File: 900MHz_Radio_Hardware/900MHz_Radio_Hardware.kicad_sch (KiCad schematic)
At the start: 9 parts, among them U1 TSR_1-2450

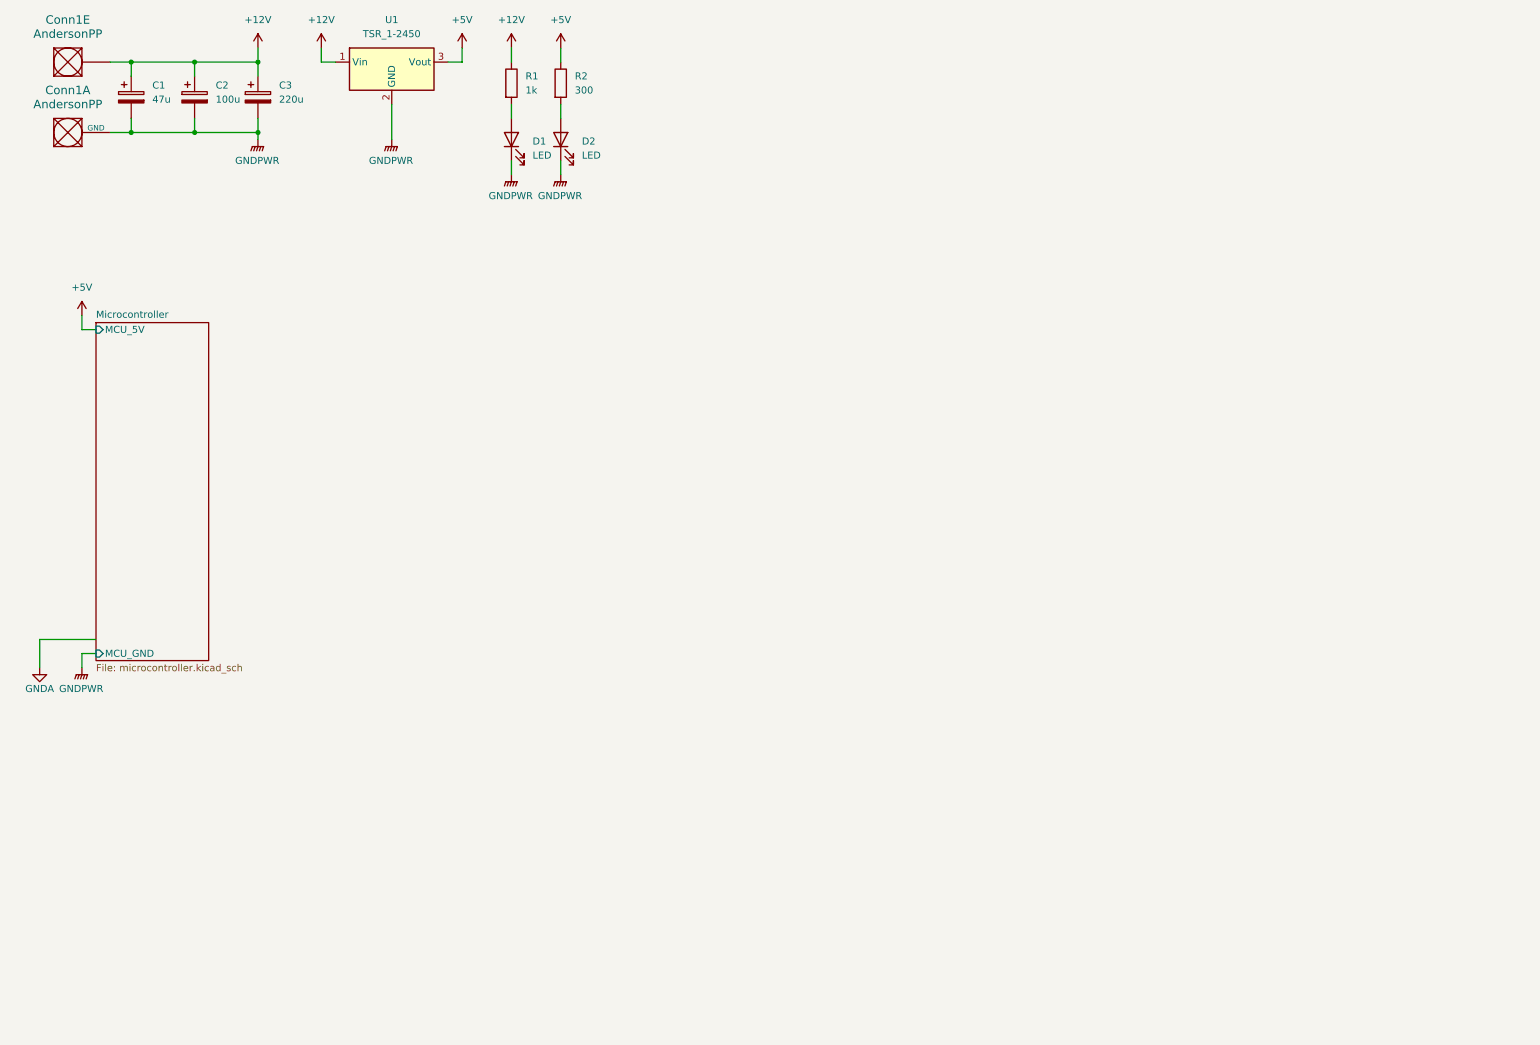
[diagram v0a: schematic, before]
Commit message: Worked on oscillator circuit
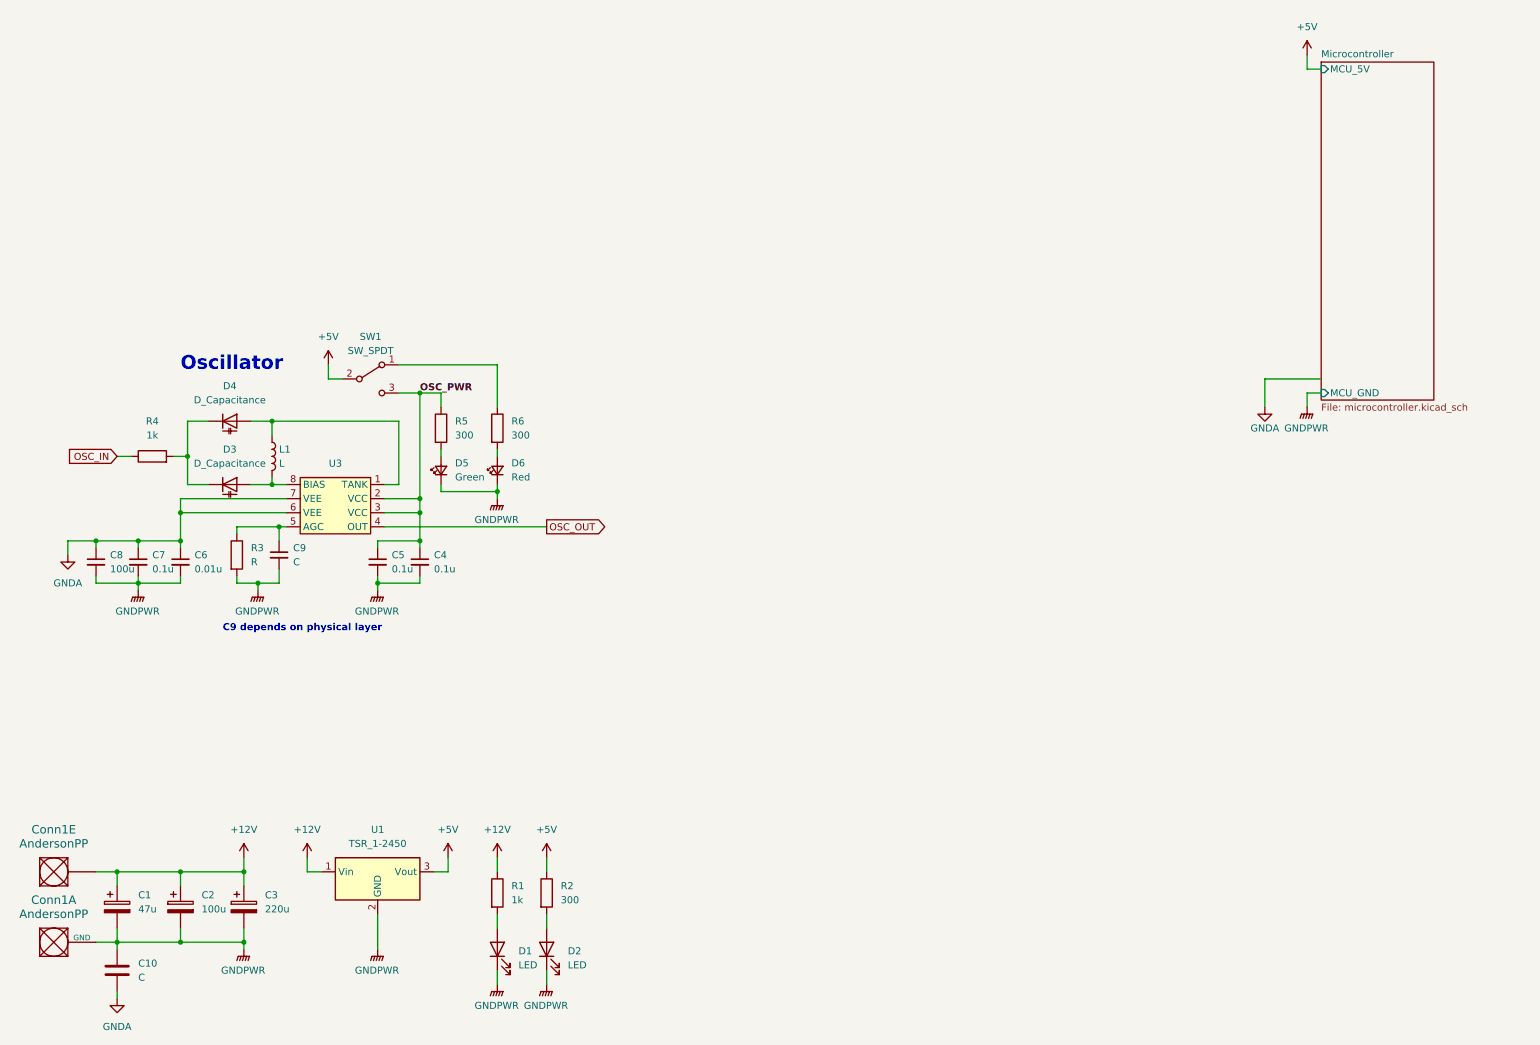
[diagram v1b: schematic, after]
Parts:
- added C10: C, symbol Device:C
- added C4, C5, C7: 0.1u, symbol Device:C_Small
- added C6: 0.01u, symbol Device:C_Small
- added C8: 100u, symbol Device:C_Small
- added C9: C, symbol Device:C_Small
- added D3, D4: D_Capacitance, symbol Device:D_Capacitance
- added D5: Green, symbol Device:LED_Small
- added D6: Red, symbol Device:LED_Small
- added L1: L, symbol Device:L
- added R3: R, symbol Device:R
- added R4: 1k, symbol Device:R
- added R5, R6: 300, symbol Device:R
- added SW1: SW_SPDT, symbol Switch:SW_SPDT
- added U3: ~, Package_SO:SOIC-8_3.9x4.9mm_P1.27mm, symbol MRDT_ICs:MC100EL1648DG
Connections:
- net +5V: now also SW1.2 (B)
- net GNDA: now also C10.2, C6.1, C7.1, C8.1, U3.6 (VEE), U3.7 (VEE)
- net GNDPWR: now also C10.1, C4.2, C5.2, C6.2, C7.2, C8.2, C9.2, D5.1 (K), D6.1 (K), R3.2
- new net: D3.1 (K), D4.1 (K), R4.2
- new net: D3.2 (A), L1.2, U3.8 (BIAS)
- new net: D6.2 (A), R6.2
- new net: D4.2 (A), L1.1, U3.1 (TANK)
- new net: C9.1, R3.1, U3.5 (AGC)
- new net: R6.1, SW1.1 (A)
- new net: D5.2 (A), R5.2
- new net OSC_IN: R4.1
- new net OSC_OUT: U3.4 (OUT)
- new net OSC_PWR: C4.1, C5.1, R5.1, SW1.3 (C), U3.2 (VCC), U3.3 (VCC)
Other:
- note added: "C9 depends on physical layer"
- note added: "Oscillator"
- moved on the sheet: C1, C2, C3, Conn1A, Conn1E, D1, D2, R1, R2, U1
